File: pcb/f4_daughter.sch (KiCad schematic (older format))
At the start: 0 parts

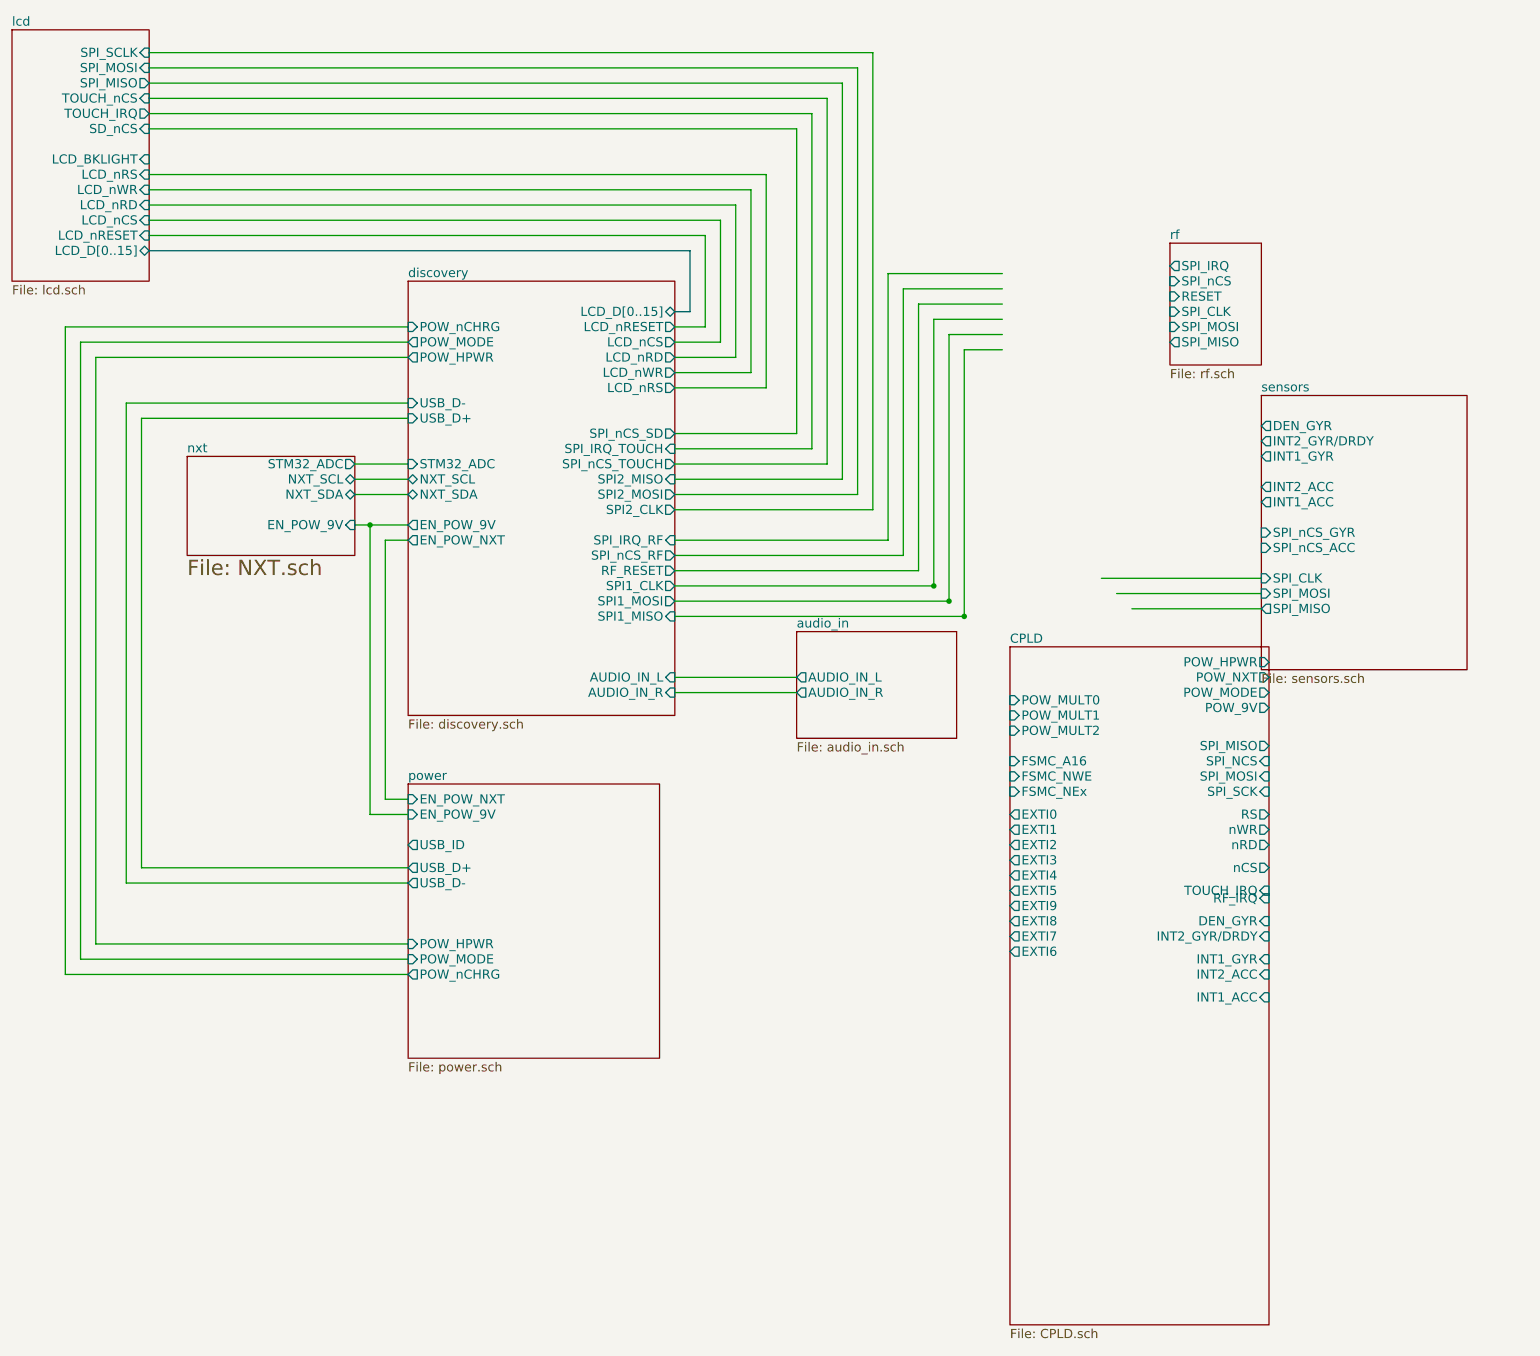
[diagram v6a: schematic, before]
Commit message: Removed the POW multiplexer lines and put the standard interrupt lines
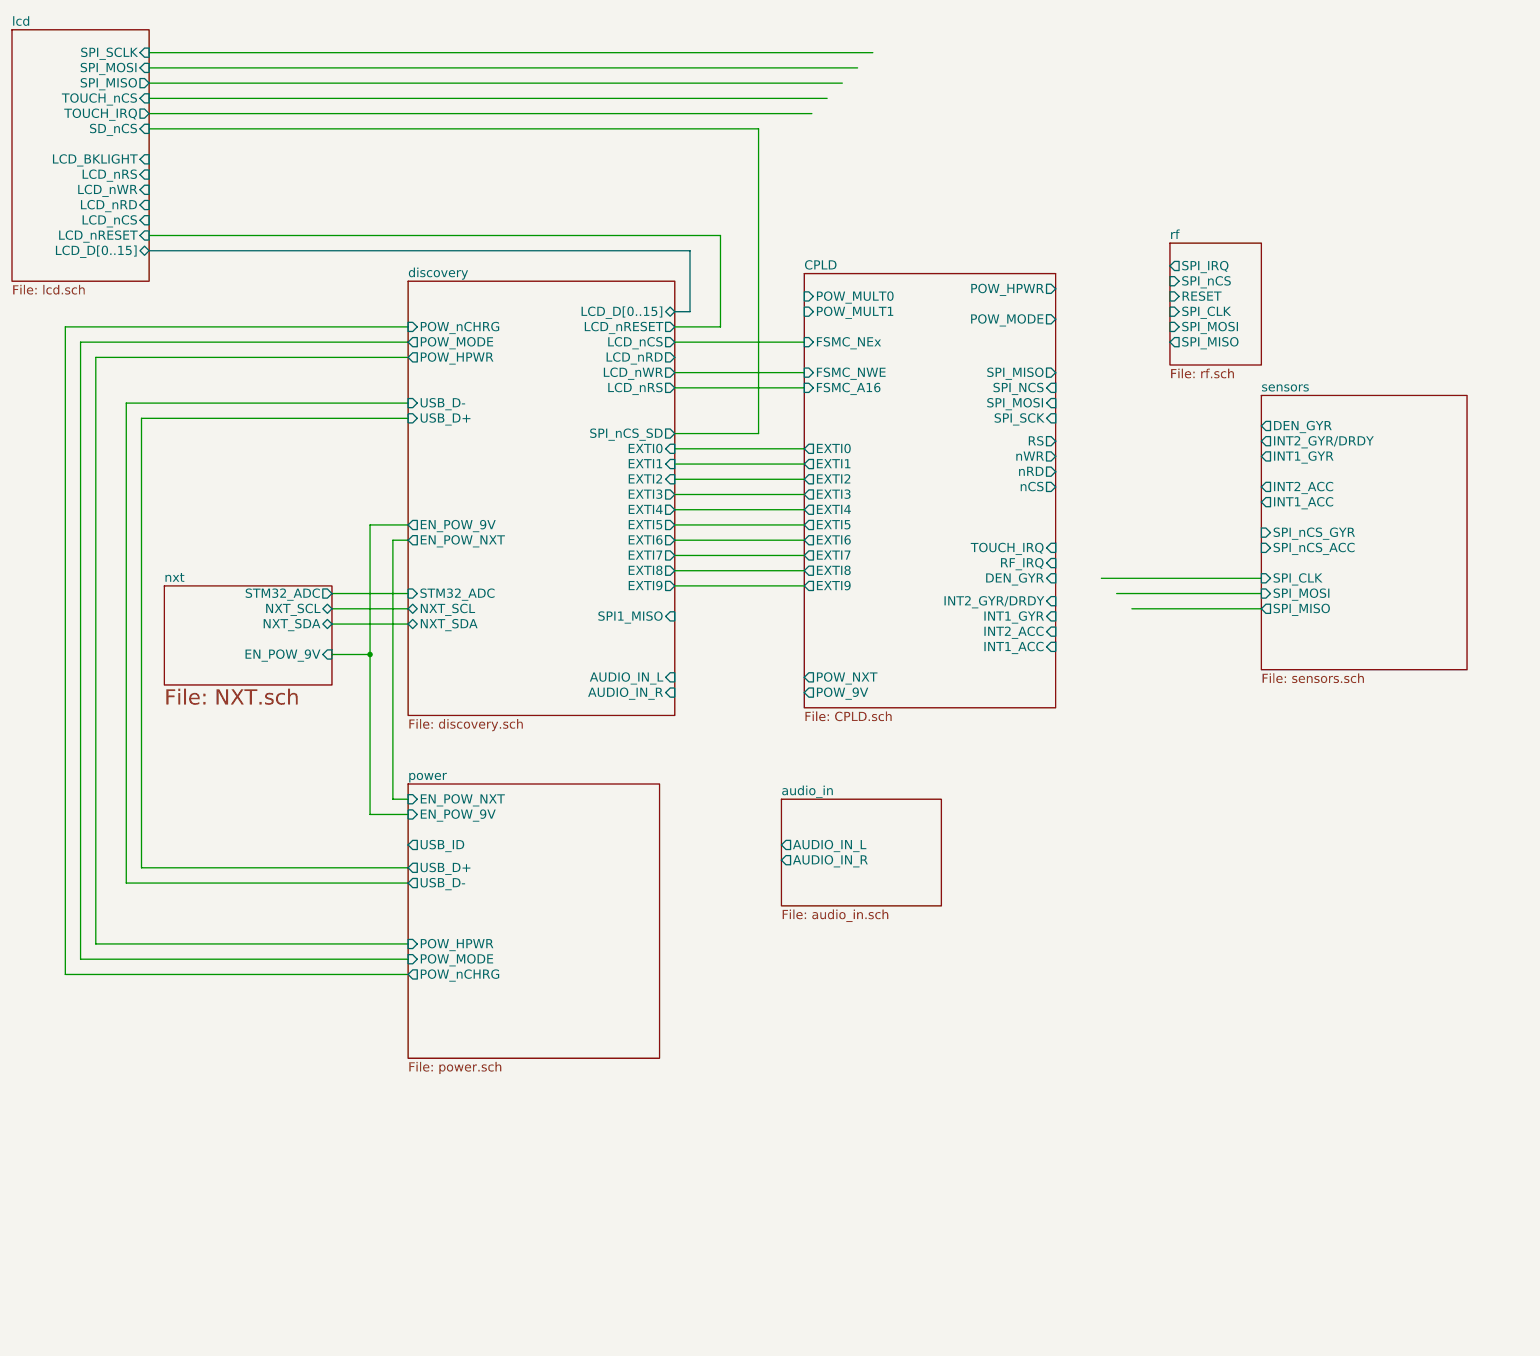
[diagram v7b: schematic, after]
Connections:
- wire segments 81 -> 52

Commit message: Rearranged all the lines except for the power lines.
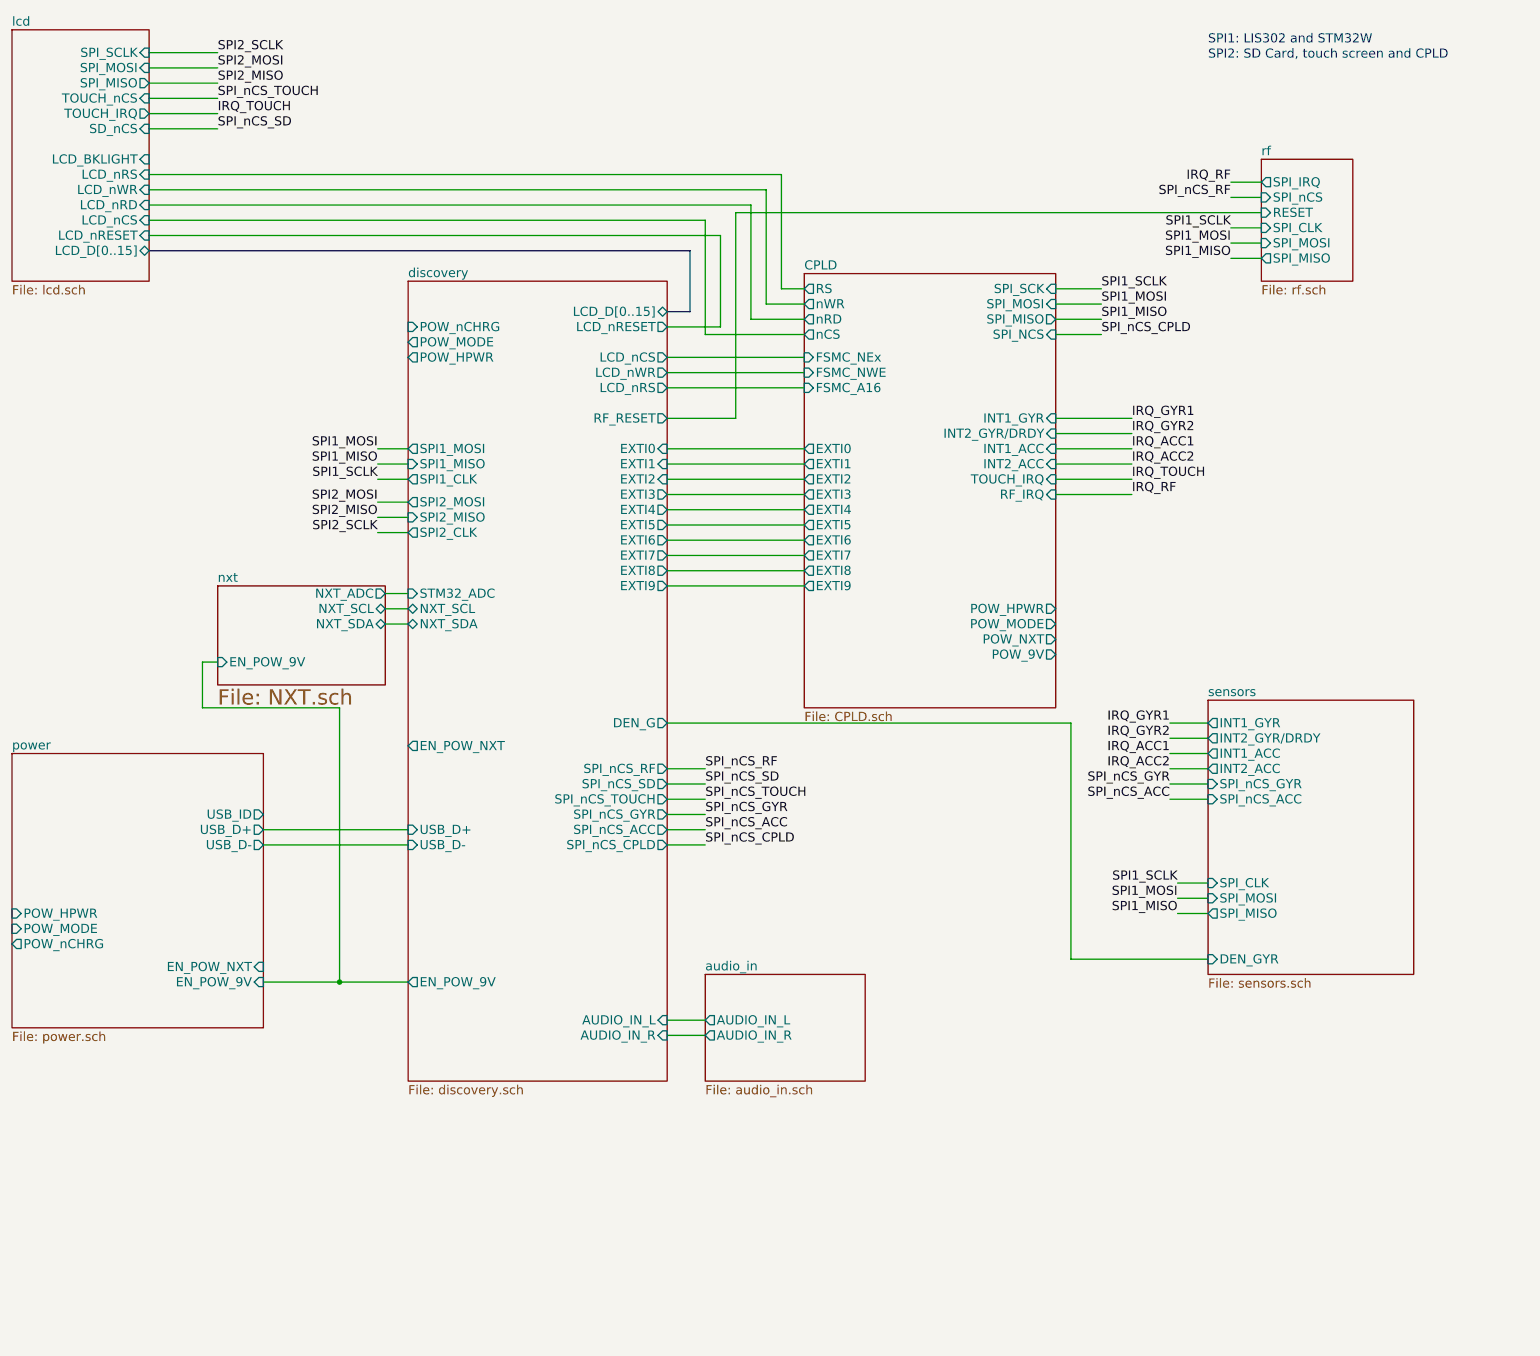
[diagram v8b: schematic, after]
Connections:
- net labels added: IRQ_ACC1, IRQ_ACC2, IRQ_GYR1, IRQ_GYR2, IRQ_RF, IRQ_TOUCH, SPI1_MISO, SPI1_MOSI, SPI1_SCLK, SPI2_MISO, SPI2_MOSI, SPI2_SCLK, SPI_nCS_ACC, SPI_nCS_CPLD, SPI_nCS_GYR, SPI_nCS_RF, SPI_nCS_SD, SPI_nCS_TOUCH
- wire segments 52 -> 88
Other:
- note added: "SPI1: LIS302 and STM32W"
- note added: "SPI2: SD Card, touch screen and CPLD"
